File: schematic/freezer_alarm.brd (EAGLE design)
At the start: 36.5 x 78.7 mm, 5 parts, among them IC1 DS18B20+, IC2 DS18B20+

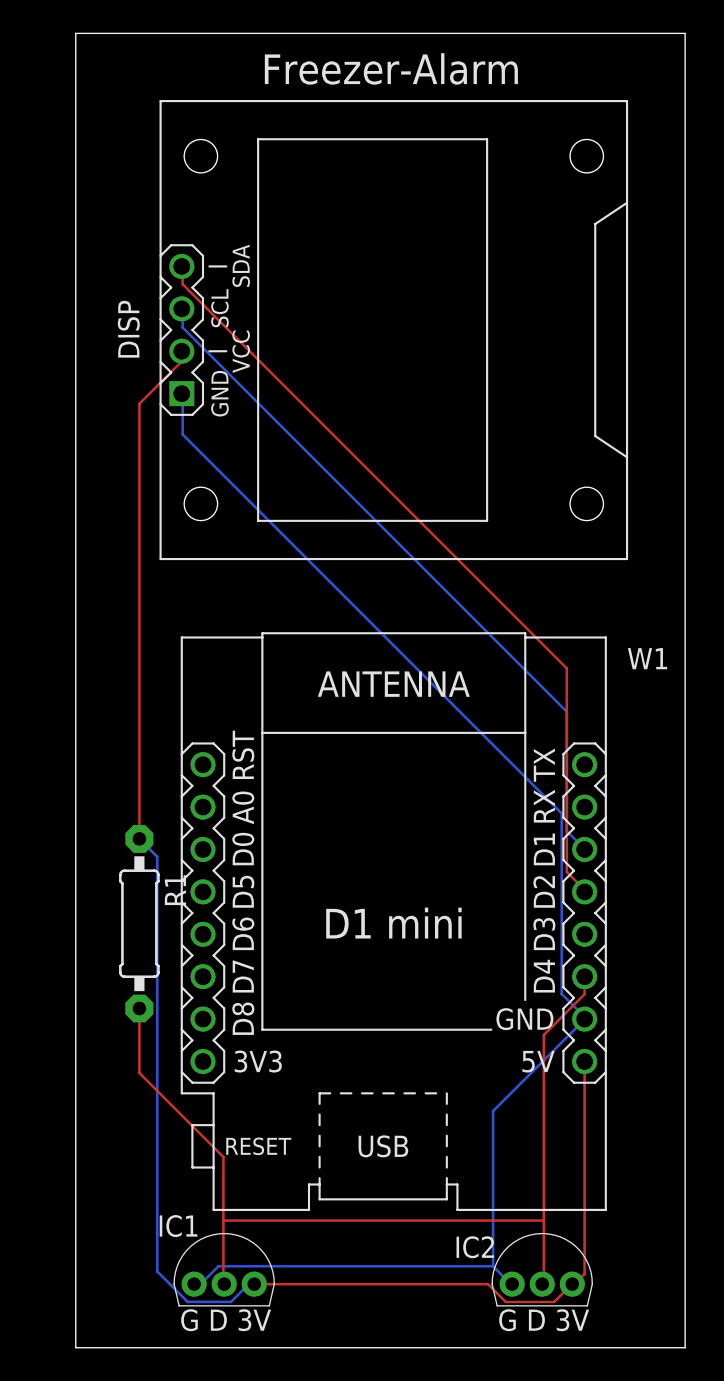
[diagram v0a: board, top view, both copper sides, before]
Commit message: Added notch for usb plug
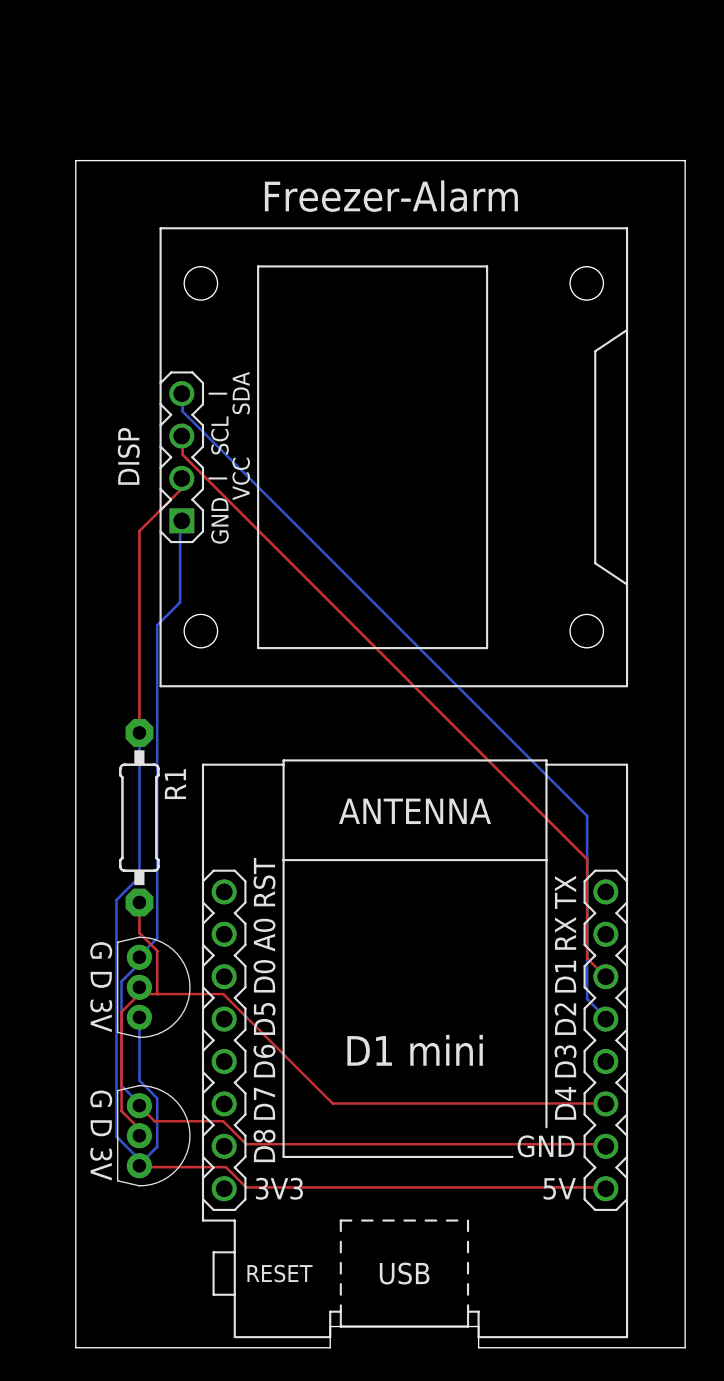
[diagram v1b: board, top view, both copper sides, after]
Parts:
- moved IC2 25.7 mm to (3.81, 12.7), turned to 180 degrees
- moved IC1 18.5 mm to (3.81, 21.6), turned to 180 degrees
- moved W1 7.73 mm to (20.3, 17.8)
- moved DISP 7.62 mm to (19.1, 53.3)
- moved R1 6.35 mm to (3.81, 31.8)
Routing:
- net GND: track 84.5 -> 66.0 mm
- net +5V: track 97.3 -> 81.8 mm
- net 1-WIRE: track 57.4 -> 46.7 mm
- net SCL: track 42.4 -> 42.9 mm
- net SDA: track 47.5 -> 48.0 mm
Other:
- board size 36.5 x 78.7 mm -> 36.5 x 71.1 mm

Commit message: Moved arrduino files to src
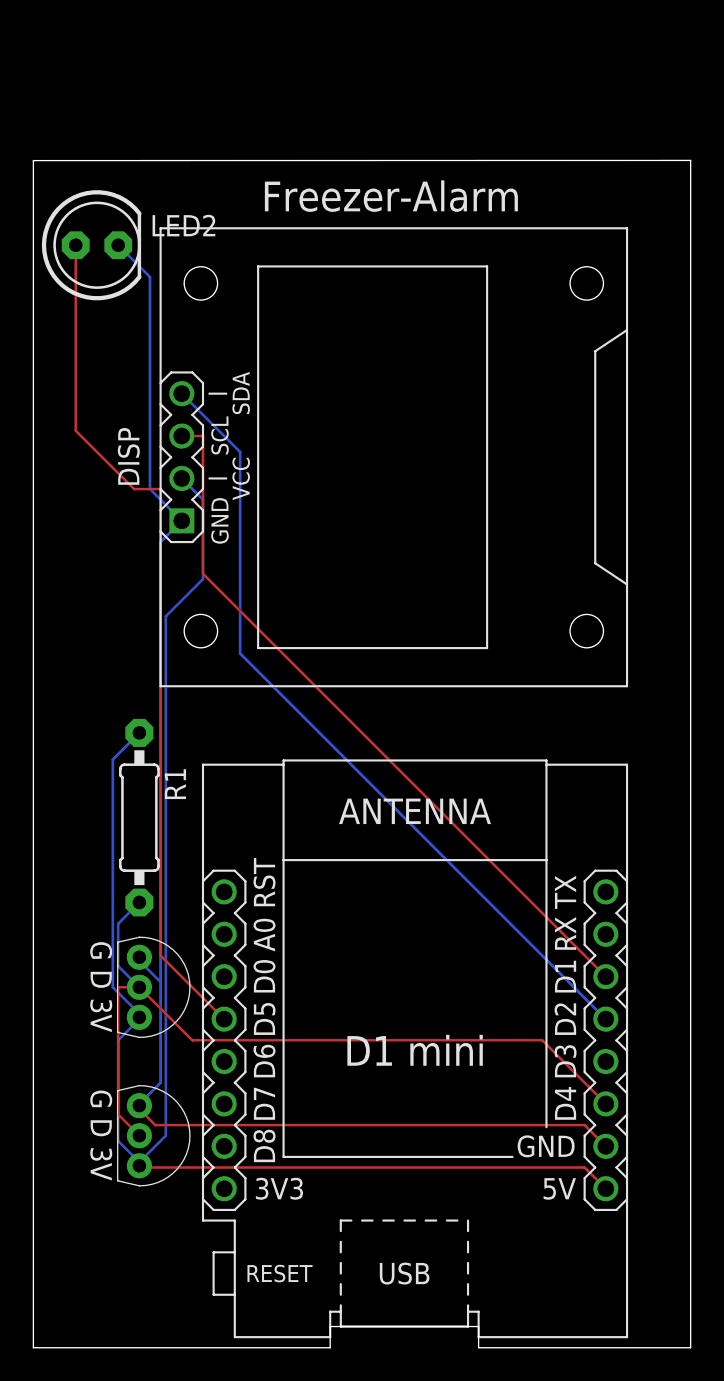
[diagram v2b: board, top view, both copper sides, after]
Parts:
- added LED2: (no value), adafruit:LED5MM
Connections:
- new net N$1: LED2.A, W1.JP1.4
- net GND: now also LED2.K
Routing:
- net N$1: track 0.00 -> 51.0 mm
- net GND: track 66.0 -> 85.3 mm
- net +5V: track 81.8 -> 99.9 mm
- net 1-WIRE: track 46.7 -> 47.7 mm
- net SCL: track 42.9 -> 43.6 mm
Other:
- board size 36.5 x 71.1 mm -> 39.4 x 71.1 mm

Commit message: Added R2
Added R2
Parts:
- added R2: 1K, adafruit:0207/10
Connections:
- new net N$2: LED2.K, R2.1
- net GND: now also R2.2; no longer LED2.K
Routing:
- net N$2: track 0.00 -> 18.0 mm
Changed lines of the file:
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@@
 <?xml version="1.0" encoding="utf-8"?>
 <!DOCTYPE eagle SYSTEM "eagle.dtd">
-<eagle version="9.3.2">
+<eagle version="9.6.2">
 <drawing>
 <settings>
@@
 <attribute name="VALUE" x="4.4704" y="64.2366" size="1.27" layer="27" ratio="10"/>
 </element>
+<element name="R2" library="adafruit" library_urn="urn:adsk.eagle:library:420" package="0207/10" package3d_urn="urn:adsk.eagle:package:6240597/1" value="1K" x="1.27" y="54.61" smashed="yes" rot="R90">
+<attribute name="NAME" x="-0.254" y="51.562" size="1.27" layer="25" ratio="10" rot="R90"/>
+<attribute name="VALUE" x="1.905" y="52.3494" size="1.27" layer="27" ratio="10" rot="R90"/>
+</element>
 </elements>
 <signals>
@@
 <contactref element="IC2" pad="1"/>
 <contactref element="W1" pad="JP2.7"/>
-<contactref element="LED2" pad="K"/>
 <wire x1="4.445" y1="51.435" x2="6.35" y2="49.53" width="0.1524" layer="16"/>
-<wire x1="4.445" y1="64.135" x2="4.445" y2="51.435" width="0.1524" layer="16"/>
-<wire x1="2.54" y1="66.04" x2="4.445" y2="64.135" width="0.1524" layer="16"/>
+<wire x1="4.445" y1="64.135" x2="4.445" y2="59.7408" width="0.1524" layer="16"/>
+<wire x1="4.445" y1="59.7408" x2="4.445" y2="51.435" width="0.1524" layer="16"/>
 <wire x1="30.48" y1="13.335" x2="31.75" y2="12.065" width="0.1524" layer="1"/>
 <wire x1="4.7625" y1="13.335" x2="30.48" y2="13.335" width="0.1524" layer="1"/>
@@
 <wire x1="5.08" y1="48.26" x2="6.35" y2="49.53" width="0.1524" layer="16"/>
 <wire x1="5.08" y1="21.9075" x2="5.08" y2="48.26" width="0.1524" layer="16"/>
+<contactref element="R2" pad="2"/>
+<wire x1="4.445" y1="59.7408" x2="1.3716" y2="59.7408" width="0.1524" layer="16"/>
+<wire x1="1.3716" y1="59.7408" x2="1.27" y2="59.69" width="0.1524" layer="16"/>
 </signal>
 <signal name="SDA">
@@
 <wire x1="0" y1="66.04" x2="0" y2="54.9275" width="0.1524" layer="1"/>
 </signal>
+<signal name="N$2">
+<contactref element="LED2" pad="K"/>
+<contactref element="R2" pad="1"/>
+<wire x1="1.2192" y1="58.2168" x2="1.2192" y2="49.53" width="0.1524" layer="16"/>
+<wire x1="0.1524" y1="59.2836" x2="1.2192" y2="58.2168" width="0.1524" layer="16"/>
+<wire x1="0.1524" y1="63.7032" x2="0.1524" y2="59.2836" width="0.1524" layer="16"/>
+<wire x1="2.4384" y1="65.9892" x2="0.1524" y2="63.7032" width="0.1524" layer="16"/>
+<wire x1="1.2192" y1="49.53" x2="1.27" y2="49.53" width="0.1524" layer="16"/>
+<wire x1="2.4384" y1="65.9892" x2="2.54" y2="66.04" width="0.1524" layer="16"/>
+</signal>
 </signals>
